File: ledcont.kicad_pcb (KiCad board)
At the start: 2 copper layers, 18.3 x 34 mm, 27 parts, among them J1 Screw_Terminal_01x02, J2 Screw_Terminal_01x02, U1 PAM2804, U2 MCP6002-xSN

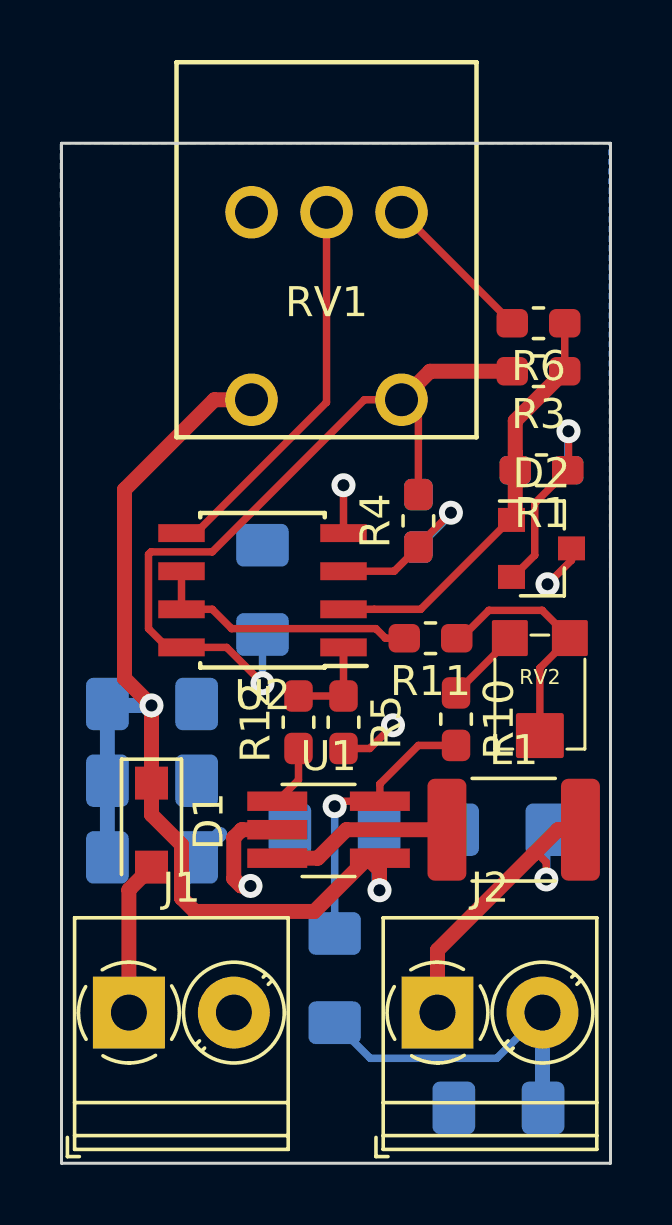
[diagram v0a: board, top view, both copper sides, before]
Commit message: More work to get things ordered.  Updated the BoM.
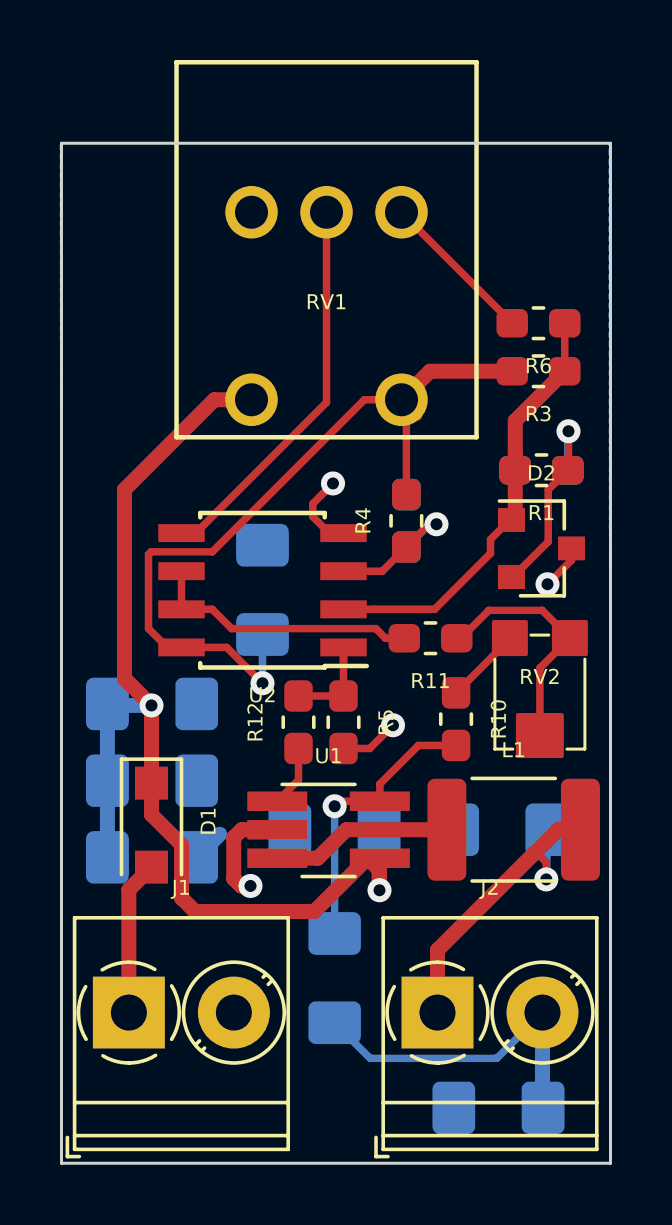
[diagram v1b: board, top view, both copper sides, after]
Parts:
- moved R4 0.40 mm to (122.3, 73.3)
- moved R7 0.40 mm to (122.3, 73.3)
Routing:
- net GND: track 10.1 -> 11.2 mm
- net Net-(R4-Pad1): track 6.54 -> 5.58 mm
